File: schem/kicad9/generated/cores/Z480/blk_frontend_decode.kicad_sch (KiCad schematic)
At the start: 0 parts

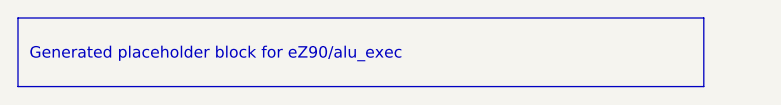
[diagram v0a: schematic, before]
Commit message: systems: rename CarbonEZ90 to CarbonZ480 and refresh maps
Detailed description:
- What changed: renamed the CarbonEZ90 system to CarbonZ480, updated system tops for Z480 tier IDs and boot signatures, refreshed memory map docs and carbon_memmap_pkg, and updated KiCad kicadgen specs plus regenerated Z480/CarbonZ480 schematics.
- Why it changed: keep system naming, maps, and schematics consistent with the new Z480 tier model.
- Files/paths affected: hdl/systems/CarbonZ480/*, hdl/systems/CarbonEZ90/* (removed), hdl/systems/CarbonZ80/*, hdl/systems/CarbonZ90/*, hdl/systems/CarbonX86/*, hdl/systems/CarbonX96/*, hdl/systems/common/rtl/carbon_memmap_pkg.sv, schem/kicad9/spec/kicadgen_*.yaml, schem/kicad9/generated/cores/Z480, schem/kicad9/generated/systems/CarbonZ480.
- Any compatibility notes: reset still enters P0; Z480 presents as P7; memory map ranges stay stable aside from naming.
- What remains TODO: update sim harnesses and documentation references to the new names.
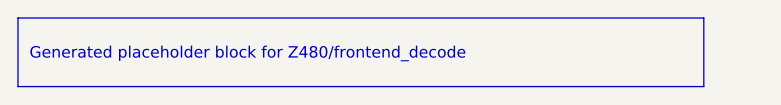
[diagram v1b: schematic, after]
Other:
- title: eZ90::alu_exec -> Z480::frontend_decode
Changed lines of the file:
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@@
 	(paper "A3")
 	(title_block
-		(title "eZ90::alu_exec")
+		(title "Z480::frontend_decode")
 		(company "Project Carbon")
 		(comment 1 "Generated - do not edit in generated/")
@@
 	)
 	(text_box
-		"Generated placeholder block for eZ90/alu_exec"
+		"Generated placeholder block for Z480/frontend_decode"
 		(exclude_from_sim no)
 		(at

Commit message: kicad: generate core-level hierarchical schematics
Detailed description:
- What changed: regenerated common and core schematics for Z85/Z90/Z380/Z480, Am9513/4/5, Am95xx, and CarbonIO/DMA placeholders
- Why it changed: update generated KiCad 9 outputs to reflect the final naming and tier model
- Files/paths affected: schem/kicad9/generated/common/* and schem/kicad9/generated/cores/*
- How to run it: scripts/gen_kicad.sh (or python tools/kicadgen/src/kicadgen.py)
- What remains TODO: regenerate and commit system-level schematics
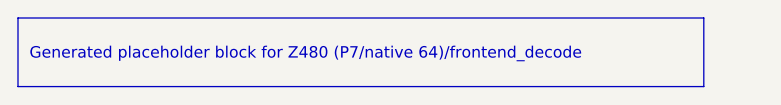
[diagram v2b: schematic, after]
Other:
- title: Z480::frontend_decode -> Z480 (P7/native 64)::frontend_decode
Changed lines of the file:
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@@
 	(version 20250114)
 	(generator "kicadgen")
-	(generator_version "0.1")
+	(generator_version "0.2")
 	(paper "A3")
 	(title_block
-		(title "Z480::frontend_decode")
+		(title "Z480 (P7/native 64)::frontend_decode")
 		(company "Project Carbon")
 		(comment 1 "Generated - do not edit in generated/")
@@
 	)
 	(text_box
-		"Generated placeholder block for Z480/frontend_decode"
+		"Generated placeholder block for Z480 (P7/native 64)/frontend_decode"
 		(exclude_from_sim no)
 		(at
